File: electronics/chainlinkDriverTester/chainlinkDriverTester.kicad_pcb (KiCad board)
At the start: 2 copper layers, 198.1 x 95.2 mm, 151 parts, among them J1 Barrel_Jack_Switch, J10 Sensor C, J11 Sensor D, J12 Motor E, J13 Motor F, J14 Sensor E, J15 Sensor F, J2 Conn_01x03_Female, J22 Power, J26 exp, J27 exp, J28 exp, J29 exp, J3 Motor A, J30 exp, J31 exp, J32 Conn_01x06_Female, J5 Motor B, J6 Motor C, J7 Motor D, J8 Sensor A, J9 Sensor B, U1 AP7361C-33E, U2 TTGO_TDisplay, U3 VN7007ALH, U4 MCP23017_SS, U5 INA219BxD, U6 SN74LV1T34DBV, U7 Buck

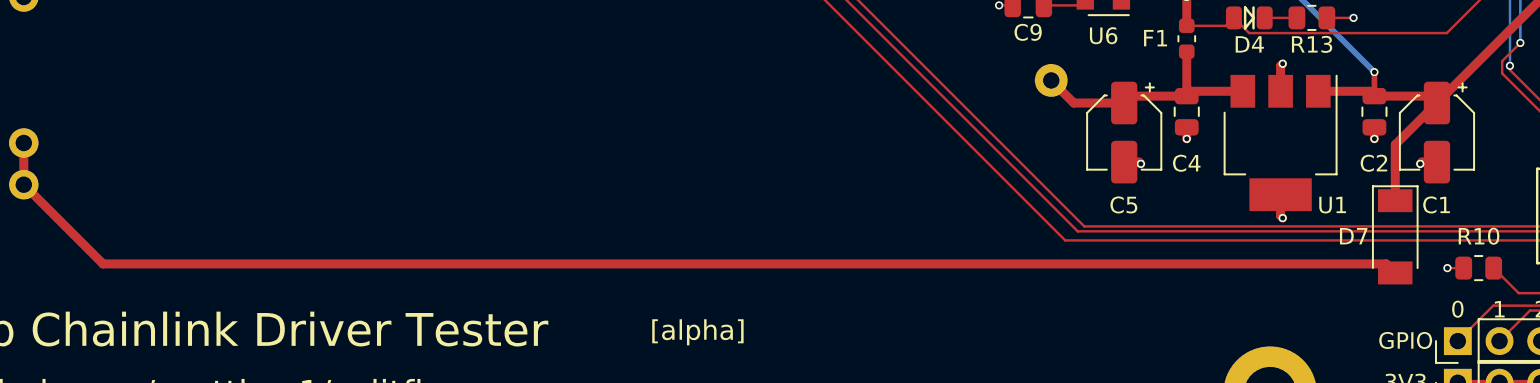
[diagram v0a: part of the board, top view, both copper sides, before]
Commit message: Fix DRC error on chainlinkDriverTester, run BOM generation for chainlinkDriver
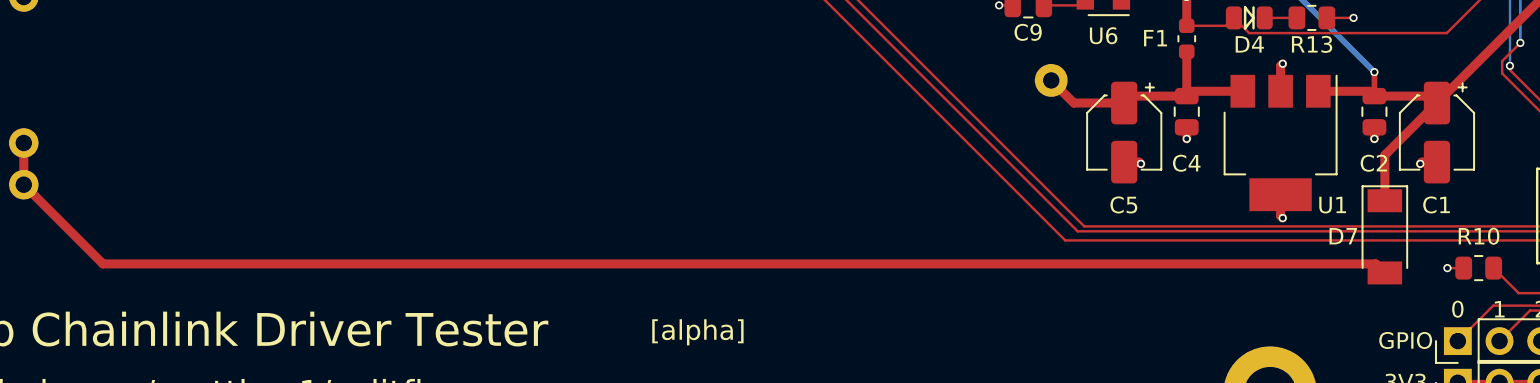
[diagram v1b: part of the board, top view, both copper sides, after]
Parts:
- moved D7 0.64 mm to (131.4, 107.3)
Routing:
- net Net-(D7-Pad2): track 88.3 -> 87.7 mm
